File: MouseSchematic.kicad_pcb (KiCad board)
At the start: 2 copper layers, 83.2 x 82.7 mm, 69 parts, among them IC1 AZ1117IH-3.3TRG1, J1 Right Header, J2 Left Header, J4 JST1, J5 JST2, J6 Programming Header, Q1 IR Receiver, Q2 IR Receiver, Q3 IR Receiver, Q4 IR Receiver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

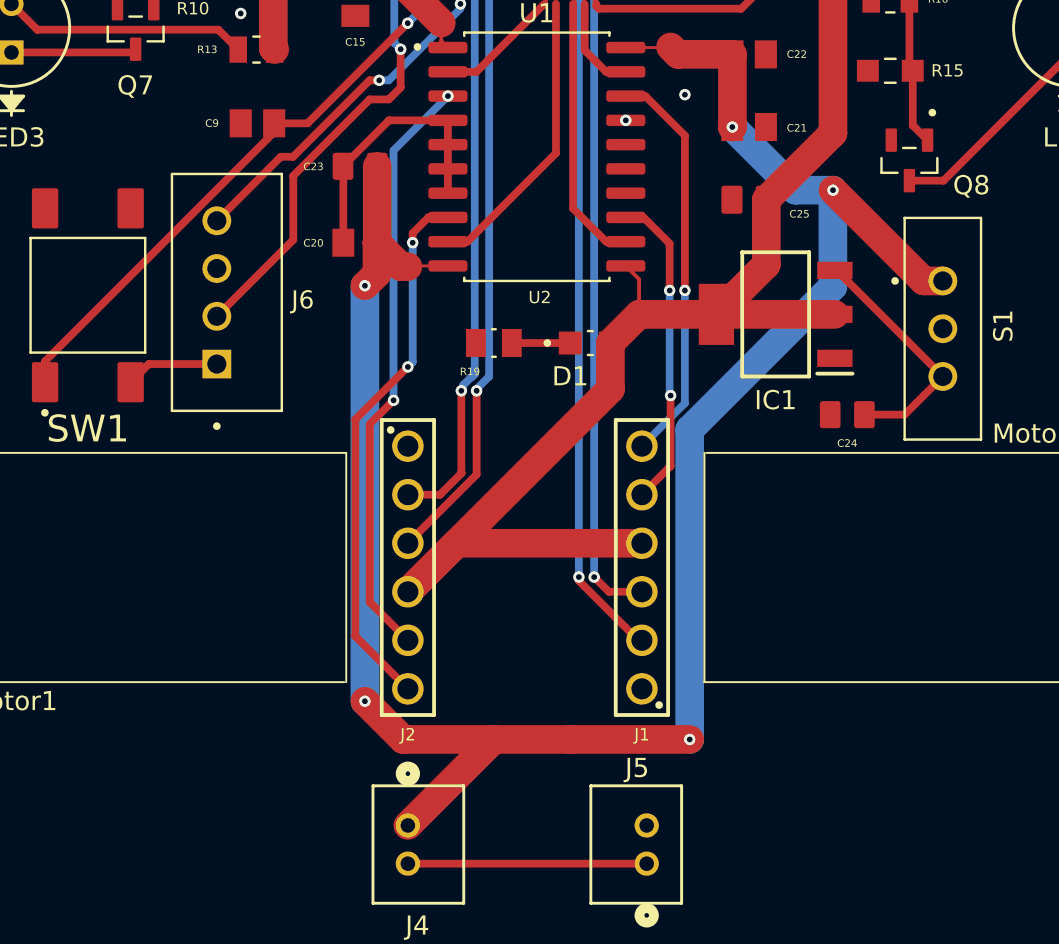
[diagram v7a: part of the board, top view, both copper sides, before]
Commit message: Finished PCB with MGND issue fixed and edge cuts for battery holders
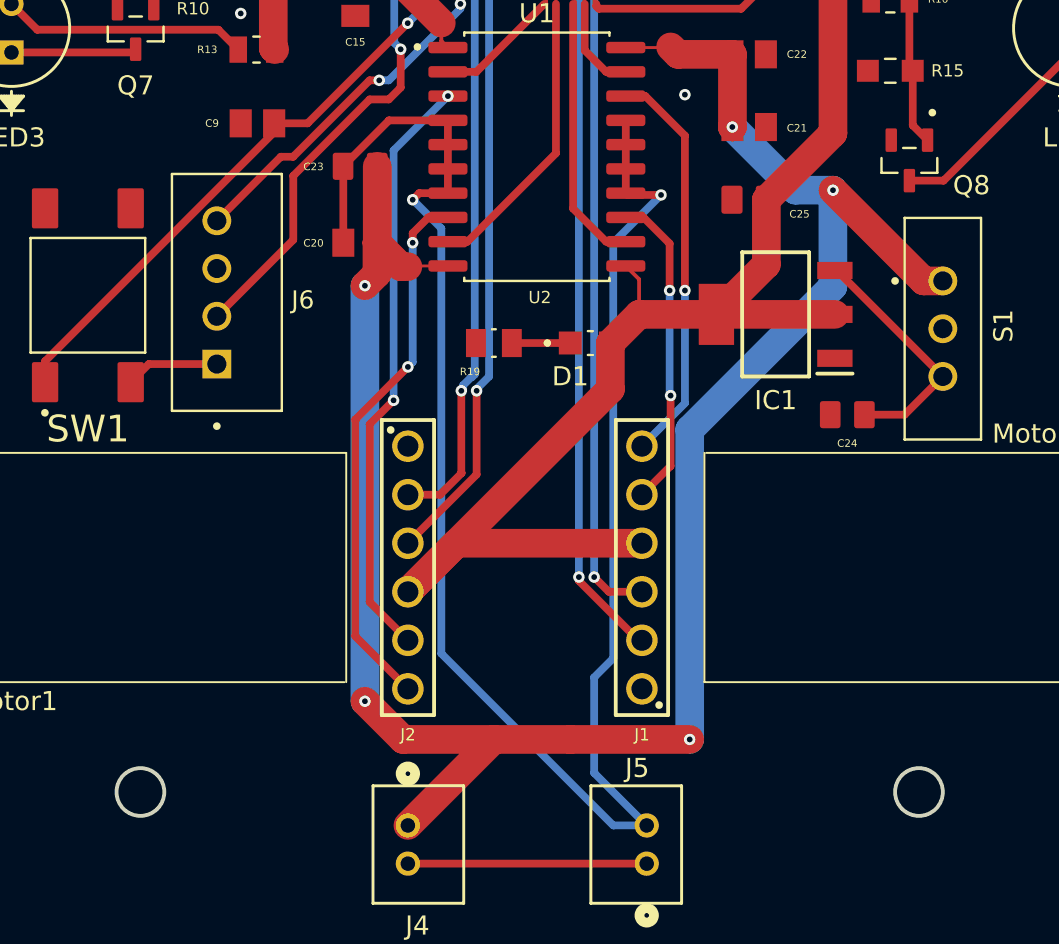
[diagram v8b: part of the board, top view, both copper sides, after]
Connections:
- C20 pad 1: GND -> MGND
- C23 pad 1: GND -> MGND
- J5 pad 2: GND -> MGND
- U2 pad 14: GND -> MGND
- U2 pad 15: GND -> MGND
- U2 pad 16: GND -> MGND
- U2 pad 17: GND -> MGND
- U2 pad 4: GND -> MGND
- U2 pad 5: GND -> MGND
- U2 pad 6: GND -> MGND
- U2 pad 7: GND -> MGND
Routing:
- net MGND: track 0.00 -> 96.4 mm, vias 0 -> 2
- net GND: track 35.7 -> 21.4 mm, vias 8 -> 7
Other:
- outline, holes or cut-outs redrawn
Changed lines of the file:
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@@
 	(net 79 "unconnected-(U1-PB11-Pad30)")
 	(net 80 "unconnected-(U1-PH0-Pad5)")
+	(net 81 "MGND")
 	(footprint "C0805C104K5RACTU:CAPC2012X88N"
 		(layer "F.Cu")
@@
 			(size 1.15 1.47)
 			(layers "F.Cu" "F.Mask" "F.Paste")
-			(net 1 "GND")
+			(net 81 "MGND")
 			(pintype "passive")
 			(solder_mask_margin 0.102)
@@
 			(layers "F.Cu" "F.Mask" "F.Paste")
 			(roundrect_rratio 0.25)
-			(net 1 "GND")
+			(net 81 "MGND")
 			(pinfunction "GND")
 			(pintype "power_in")
@@
 			(layers "F.Cu" "F.Mask" "F.Paste")
 			(roundrect_rratio 0.25)
-			(net 1 "GND")
+			(net 81 "MGND")
 			(pinfunction "GND")
 			(pintype "power_in")
@@
 			(layers "F.Cu" "F.Mask" "F.Paste")
 			(roundrect_rratio 0.25)
-			(net 1 "GND")
+			(net 81 "MGND")
 			(pinfunction "GND")
 			(pintype "power_in")
@@
 			(layers "F.Cu" "F.Mask" "F.Paste")
 			(roundrect_rratio 0.25)
-			(net 1 "GND")
+			(net 81 "MGND")
 			(pinfunction "GND")
 			(pintype "power_in")
@@
 			(layers "F.Cu" "F.Mask" "F.Paste")
 			(roundrect_rratio 0.25)
-			(net 1 "GND")
+			(net 81 "MGND")
 			(pinfunction "GND")
 			(pintype "power_in")
@@
 			(layers "F.Cu" "F.Mask" "F.Paste")
 			(roundrect_rratio 0.25)
-			(net 1 "GND")
+			(net 81 "MGND")
 			(pinfunction "GND")
 			(pintype "power_in")
@@
 			(layers "F.Cu" "F.Mask" "F.Paste")
 			(roundrect_rratio 0.25)
-			(net 1 "GND")
+			(net 81 "MGND")
 			(pinfunction "GND")
 			(pintype "power_in")
@@
 			(layers "F.Cu" "F.Mask" "F.Paste")
 			(roundrect_rratio 0.25)
-			(net 1 "GND")
+			(net 81 "MGND")
 			(pinfunction "GND")
 			(pintype "power_in")
@@
 			(layers "F.Cu" "F.Mask" "F.Paste")
 			(roundrect_rratio 0.125)
-			(net 1 "GND")
+			(net 81 "MGND")
 			(pintype "passive")
 			(solder_mask_margin 0.102)
@@
 			(layers "*.Cu" "*.Mask")
 			(remove_unused_layers no)
-			(net 1 "GND")
+			(net 81 "MGND")
 			(pinfunction "2")
 			(pintype "unspecified")
@@
 		(layer "Edge.Cuts")
 	)
+	(gr_circle
+		(center 179.25 139.75)
+		(end 179.25 138.5)
+		(stroke
+			(width 0.2)
+			(type solid)
+		)
+		(fill no)
+		(layer "Edge.Cuts")
+	)
 	(gr_line
 		(start 117.93629 113.64035)
@@
 		(layer "Edge.Cuts")
 	)
+	(gr_circle
+		(center 138.5 139.75)
+		(end 138.5 138.5)
+		(stroke
+			(width 0.2)
+			(type solid)
+		)
+		(fill no)
+		(layer "Edge.Cuts")
+	)
 	(gr_arc
 		(start 200.204058 135.954058)
@@
 	)
 	(segment
-		(start 151.51 104.595)
-		(end 154.595 104.595)
-		(width 0.4064)
-		(layer "F.Cu")
-		(net 1)
-	)
-	(segment
 		(start 164.75 82.125)
 		(end 164.595 82.125)
@@
 	)
 	(segment
-		(start 149.105 107)
-		(end 151.51 104.595)
-		(width 0.4064)
-		(layer "F.Cu")
-		(net 1)
-	)
-	(segment
 		(start 162.25 84.882284)
 		(end 162.691142 84.441142)
@@
 	)
 	(segment
-		(start 149.12 107.015)
-		(end 149.105 107)
-		(width 0.4064)
-		(layer "F.Cu")
-		(net 1)
-	)
-	(segment
 		(start 164.595 82.125)
 		(end 163.3042 83.4158)
@@
 	)
 	(segment
-		(start 154.595 104.595)
-		(end 154.595 105.865)
-		(width 0.4064)
-		(layer "F.Cu")
-		(net 1)
-	)
-	(segment
 		(start 163.3042 83.4158)
 		(end 163.3042 83.828085)
@@
 	)
 	(segment
-		(start 154.595 107.135)
-		(end 154.595 108.405)
-		(width 0.4064)
-		(layer "F.Cu")
-		(net 1)
-	)
-	(segment
 		(start 163.3042 83.828085)
 		(end 162.691142 84.441142)
@@
 	)
 	(segment
-		(start 154.595 105.865)
-		(end 154.595 107.135)
-		(width 0.4064)
-		(layer "F.Cu")
-		(net 1)
-	)
-	(segment
 		(start 162.25 88.316285)
 		(end 162.25 85.825)
@@
 		(net 1)
 	)
-	(segment
-		(start 149.12 111)
-		(end 149.12 107.015)
-		(width 0.4064)
-		(layer "F.Cu")
-		(net 1)
-	)
 	(via
 		(at 167 103.25)
@@
 	)
 	(via
-		(at 163.905 104.595)
-		(size 0.6)
-		(drill 0.3)
-		(layers "F.Cu" "B.Cu")
-		(net 1)
-	)
-	(via
 		(at 143.75 99)
 		(size 0.6)
@@
 		(net 68)
 	)
+	(segment
+		(start 153.095 108.405)
+		(end 152.75 108.75)
+		(width 0.4064)
+		(layer "F.Cu")
+		(net 81)
+	)
+	(segment
+		(start 154.595 108.405)
+		(end 153.095 108.405)
+		(width 0.4064)
+		(layer "F.Cu")
+		(net 81)
+	)
+	(segment
+		(start 151.51 104.595)
+		(end 154.595 104.595)
+		(width 0.4064)
+		(layer "F.Cu")
+		(net 81)
+	)
+	(segment
+		(start 163.905 108.405)
+		(end 164 108.5)
+		(width 0.4064)
+		(layer "F.Cu")
+		(net 81)
+	)
+	(segment
+		(start 164 108.5)
+		(end 165.75 108.5)
+		(width 0.4064)
+		(layer "F.Cu")
+		(net 81)
+	)
+	(segment
+		(start 163.905 108.405)
+		(end 163.905 104.595)
+		(width 0.4064)
+		(layer "F.Cu")
+		(net 81)
+	)
+	(segment
+		(start 149.105 107)
+		(end 151.51 104.595)
+		(width 0.4064)
+		(layer "F.Cu")
+		(net 81)
+	)
+	(segment
+		(start 149.12 107.015)
+		(end 149.105 107)
+		(width 0.4064)
+		(layer "F.Cu")
+		(net 81)
+	)
+	(segment
+		(start 154.595 104.595)
+		(end 154.595 105.865)
+		(width 0.4064)
+		(layer "F.Cu")
+		(net 81)
+	)
+	(segment
+		(start 154.595 107.135)
+		(end 154.595 108.405)
+		(width 0.4064)
+		(layer "F.Cu")
+		(net 81)
+	)
+	(segment
+		(start 154.595 105.865)
+		(end 154.595 107.135)
+		(width 0.4064)
+		(layer "F.Cu")
+		(net 81)
+	)
+	(segment
+		(start 149.12 111)
+		(end 149.12 107.015)
+		(width 0.4064)
+		(layer "F.Cu")
+		(net 81)
+	)
+	(via
+		(at 152.75 108.75)
+		(size 0.6)
+		(drill 0.3)
+		(layers "F.Cu" "B.Cu")
+		(net 81)
+	)
+	(via
+		(at 165.75 108.5)
+		(size 0.6)
+		(drill 0.3)
+		(layers "F.Cu" "B.Cu")
+		(net 81)
+	)
+	(segment
+		(start 165.75 108.5)
+		(end 163.25 111)
+		(width 0.4064)
+		(layer "B.Cu")
+		(net 81)
+	)
+	(segment
+		(start 163.249999 141.499999)
+		(end 165 141.499999)
+		(width 0.4064)
+		(layer "B.Cu")
+		(net 81)
+	)
+	(segment
+		(start 162.25 133.75)
+		(end 162.25 138.749999)
+		(width 0.4064)
+		(layer "B.Cu")
+		(net 81)
+	)
+	(segment
+		(start 163.25 111)
+		(end 163.25 132.75)
+		(width 0.4064)
+		(layer "B.Cu")
+		(net 81)
+	)
+	(segment
+		(start 163.25 132.75)
+		(end 162.25 133.75)
+		(width 0.4064)
+		(layer "B.Cu")
+		(net 81)
+	)
+	(segment
+		(start 154.25 132.5)
+		(end 163.249999 141.499999)
+		(width 0.4064)
+		(layer "B.Cu")
+		(net 81)
+	)
+	(segment
+		(start 152.75 108.75)
+		(end 154.25 110.25)
+		(width 0.4064)
+		(layer "B.Cu")
+		(net 81)
+	)
+	(segment
+		(start 162.25 138.749999)
+		(end 165 141.499999)
+		(width 0.4064)
+		(layer "B.Cu")
+		(net 81)
+	)
+	(segment
+		(start 154.25 110.25)
+		(end 154.25 132.5)
+		(width 0.4064)
+		(layer "B.Cu")
+		(net 81)
+	)
 	(zone
